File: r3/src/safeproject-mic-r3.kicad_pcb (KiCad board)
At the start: 2 copper layers, 30.5 x 22 mm, 23 parts, among them J101 2842142-4, U101 PCMD3180

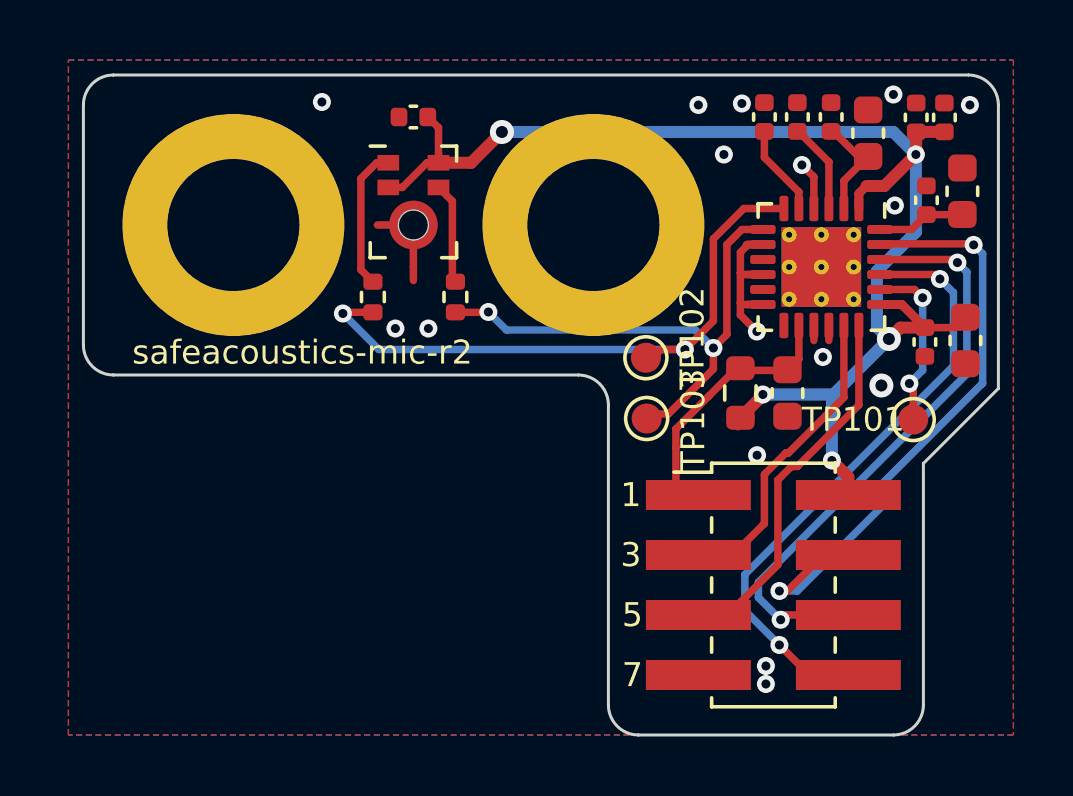
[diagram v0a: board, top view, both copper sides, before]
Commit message: Add fiducials. Change text, move to mask layer.
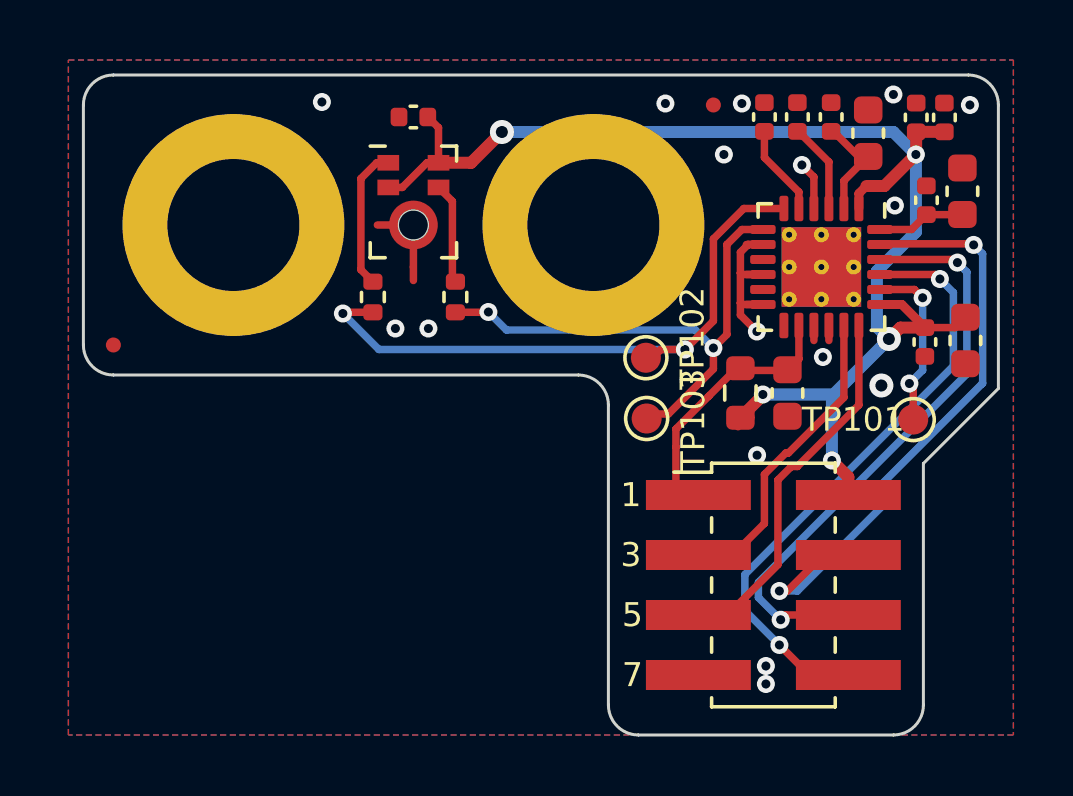
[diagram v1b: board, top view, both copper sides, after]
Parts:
- added FID1: Fiducial, Fiducial:Fiducial_0.5mm_Mask1mm, F.Cu at (10.0, -4.00)
- added FID2: Fiducial, Fiducial:Fiducial_0.5mm_Mask1mm, F.Cu at (-10.0, 4.00)
- C112: value 10uF -> 1uF
- R103: value 10k -> 100k
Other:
- board text added: "bugg-mic-r3"
- board text removed: "safeacoustics-mic-r2"

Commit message: Connect Wurth spacer mounting pads to GND
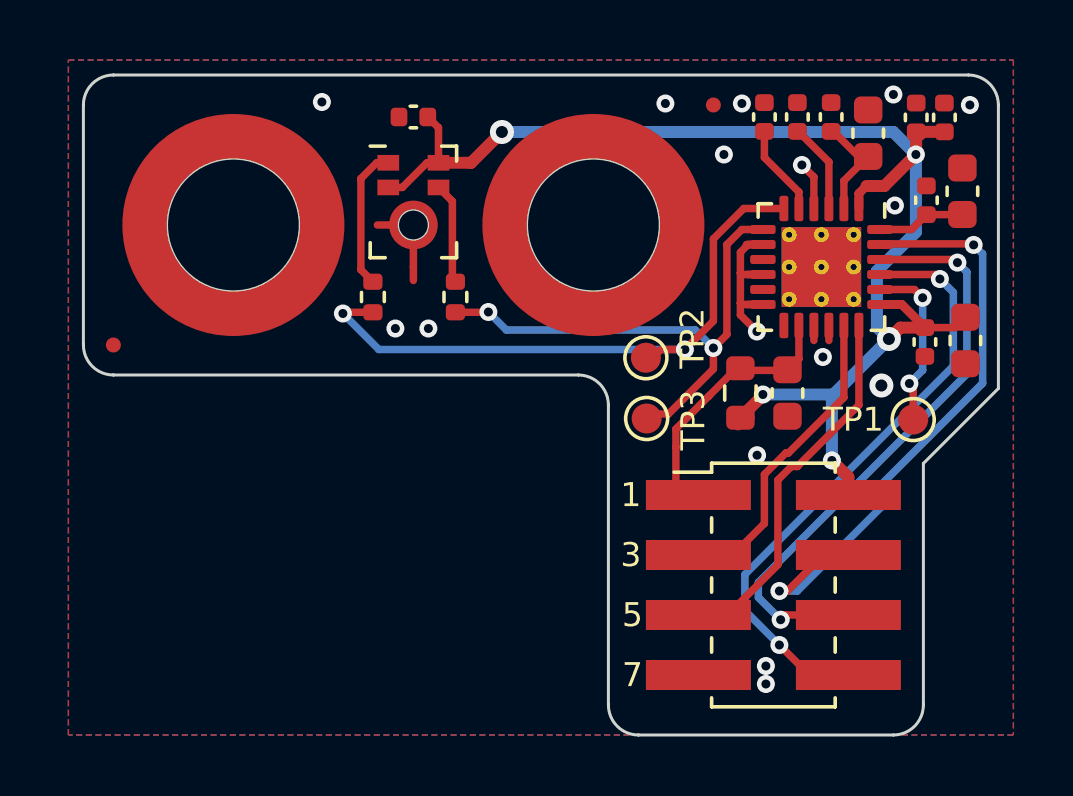
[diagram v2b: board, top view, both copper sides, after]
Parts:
- H101, H102: footprint jeffmakes-footprints:wurth-spacer-WA-SMSI-9774070360R -> Mounting_Wuerth:Mounting_Wuerth_WA-SMSI-M3_H7mm_9774070360
- renumbered TP101 to TP1, TP102 to TP2, TP103 to TP3

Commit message: Shorten test point names
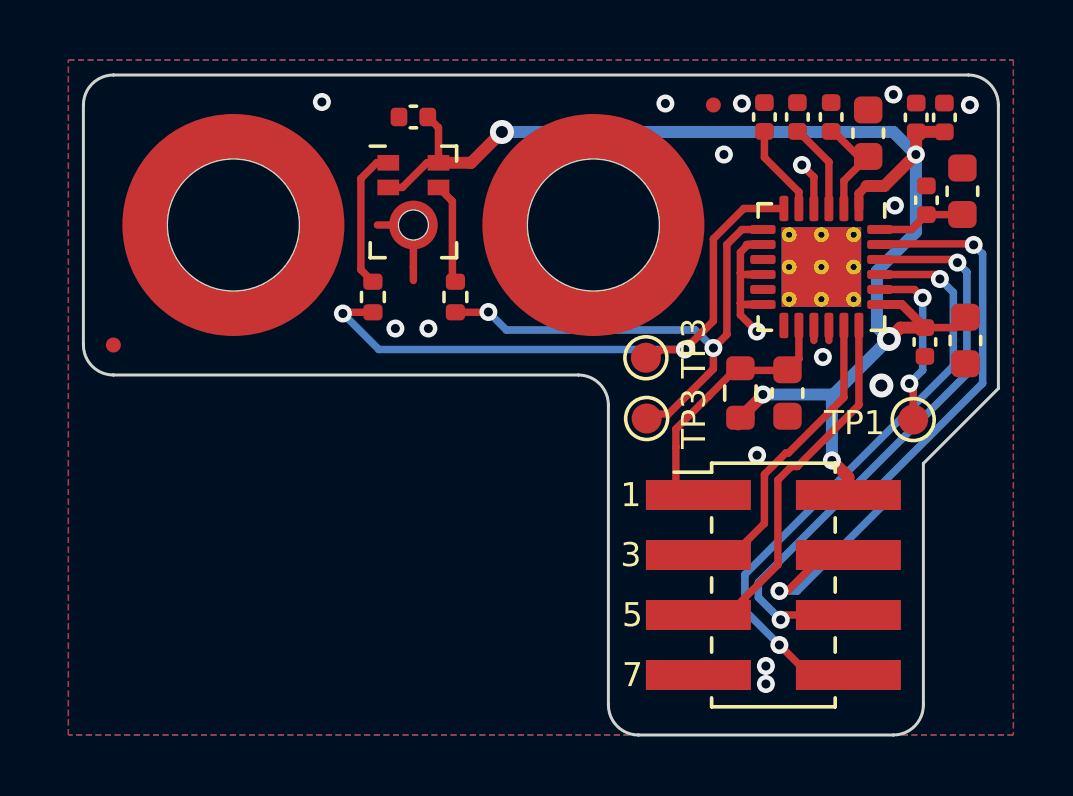
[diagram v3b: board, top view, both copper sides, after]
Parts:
- renumbered TP1 to TP101, TP2 to TP102, TP3 to TP103
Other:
- board text added: "TP1"
- board text added: "TP3"
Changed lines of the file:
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@@
   (net 18 "unconnected-(U101-Pad11)")
   (net 19 "unconnected-(U101-Pad13)")
-  (net 20 "Net-(TP1-Pad1)")
+  (net 20 "Net-(TP101-Pad1)")
   (footprint "Capacitor_SMD:C_0402_1005Metric" (layer "F.Cu")
     (at 12.8 -3.6 -90)
@@
     (property "Sheetname" "")
     (attr exclude_from_pos_files)
-    (fp_text reference "TP1" (at -2 0) (layer "F.SilkS")
+    (fp_text reference "TP101" (at -2 0) (layer "F.SilkS") hide
       (effects (font (size 0.8 0.8) (thickness 0.15)))
     )
@@
     (fp_circle (center 0 0) (end 1 0) (layer "F.CrtYd") (width 0.05) (fill none))
     (pad "1" smd circle locked (at 0 0) (size 1 1) (layers "F.Cu" "F.Mask")
-      (net 20 "Net-(TP1-Pad1)") (pinfunction "1") (pintype "passive"))
+      (net 20 "Net-(TP101-Pad1)") (pinfunction "1") (pintype "passive"))
   )
   (footprint "Capacitor_SMD:C_0603_1608Metric" (layer "F.Cu")
@@
     (property "Sheetname" "")
     (attr exclude_from_pos_files)
-    (fp_text reference "TP3" (at 1.55 0.05 90) (layer "F.SilkS")
+    (fp_text reference "TP103" (at 1.55 0.05 90) (layer "F.SilkS") hide
       (effects (font (size 0.8 0.8) (thickness 0.15)))
     )
@@
       (net 3 "+3V3") (pinfunction "IOVDD") (pintype "power_in"))
     (pad "20" smd roundrect locked (at 0.75 -1.95 270) (size 0.3 0.85) (layers "F.Cu" "F.Paste" "F.Mask") (roundrect_rratio 0.25)
-      (net 20 "Net-(TP1-Pad1)") (pinfunction "GPIO1") (pintype "bidirectional"))
+      (net 20 "Net-(TP101-Pad1)") (pinfunction "GPIO1") (pintype "bidirectional"))
     (pad "21" smd roundrect locked (at 0.25 -1.95 270) (size 0.3 0.85) (layers "F.Cu" "F.Paste" "F.Mask") (roundrect_rratio 0.25)
       (net 7 "/SDOUT") (pinfunction "SDOUT") (pintype "output"))
@@
     (property "Sheetname" "")
     (attr exclude_from_pos_files)
-    (fp_text reference "TP2" (at 1.55 -0.65 90) (layer "F.SilkS")
+    (fp_text reference "TP102" (at 1.55 -0.65 90) (layer "F.SilkS") hide
       (effects (font (size 0.8 0.8) (thickness 0.15)))
     )
@@
   (gr_line (start -11 4) (end -11 -4) (layer "Edge.Cuts") (width 0.1))
   (gr_circle (center 0 0) (end 3 0) (layer "User.1") (width 0.15) (fill none))
+  (gr_text "TP3\n" (at 9.35 4.1 90) (layer "F.SilkS")
+    (effects (font (size 0.8 0.8) (thickness 0.15)))
+  )
   (gr_text "5" (at 7.3 13) (layer "F.SilkS")
     (effects (font (size 0.8 0.8) (thickness 0.15)))
@@
     (effects (font (size 0.8 0.8) (thickness 0.15)))
   )
+  (gr_text "TP3\n" (at 9.35 6.45 90) (layer "F.SilkS")
+    (effects (font (size 0.8 0.8) (thickness 0.15)))
+  )
   (gr_text "3" (at 7.25 11) (layer "F.SilkS")
     (effects (font (size 0.8 0.8) (thickness 0.15)))
   )
+  (gr_text "TP1" (at 14.7 6.6) (layer "F.SilkS")
+    (effects (font (size 0.8 0.8) (thickness 0.15)))
+  )

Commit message: Move fiducial and GND via out of the way of the mousebite area
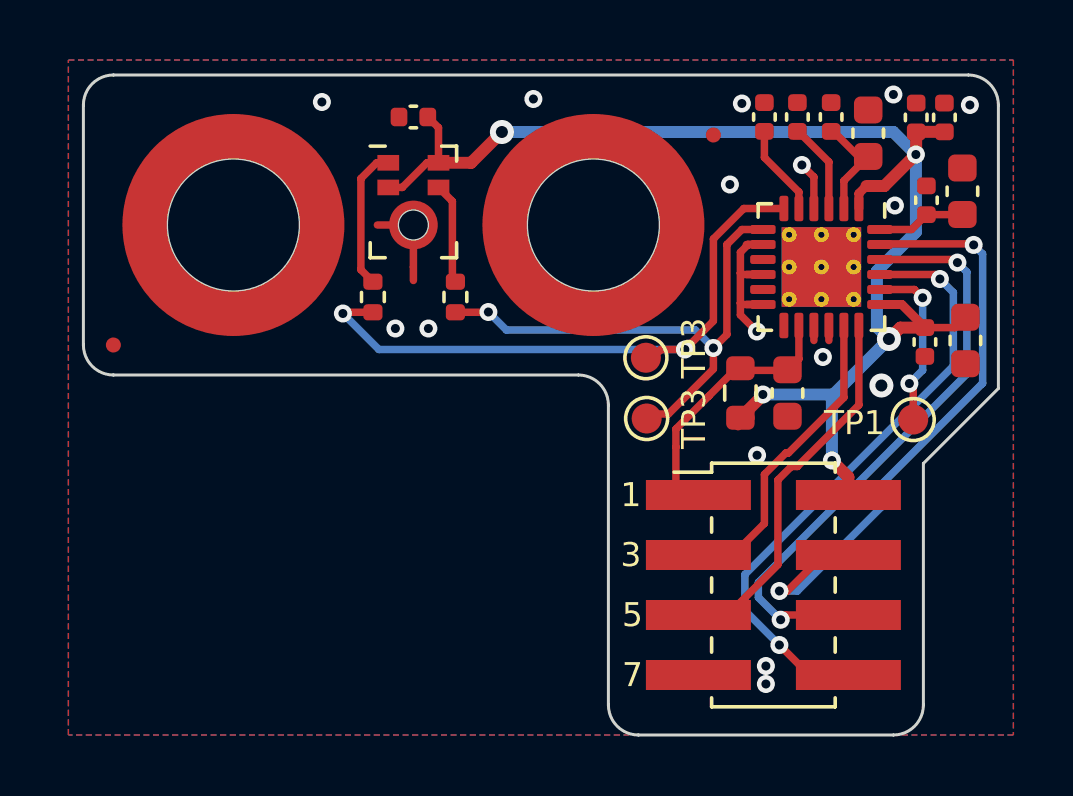
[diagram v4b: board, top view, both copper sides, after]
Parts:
- moved FID1 1.00 mm to (10.0, -3.00)
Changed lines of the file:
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@@
   )
   (footprint "Fiducial:Fiducial_0.5mm_Mask1mm" (layer "F.Cu")
-    (at 10 -4)
+    (at 10 -3)
     (descr "Circular Fiducial, 0.5mm bare copper, 1mm soldermask opening (Level C)")
     (tags "fiducial")
@@
   (via (at 11.75 15.3) (size 0.6) (drill 0.3) (layers "F.Cu" "B.Cu") (net 1))
   (via (at 16 -4.35) (size 0.6) (drill 0.3) (layers "F.Cu" "B.Cu") (net 1))
-  (via (at 10.35 -2.35) (size 0.6) (drill 0.3) (layers "F.Cu" "B.Cu") (net 1))
+  (via (at 10.55 -1.35) (size 0.6) (drill 0.3) (layers "F.Cu" "B.Cu") (net 1))
   (via (at -3.05 -4.1) (size 0.6) (drill 0.3) (layers "F.Cu" "B.Cu") (net 1))
   (via (at 16.04999 -0.65) (size 0.6) (drill 0.3) (layers "F.Cu" "B.Cu") (net 1))
   (via (at 18.55 -4) (size 0.6) (drill 0.3) (layers "F.Cu" "B.Cu") (net 1))
   (via (at 11.455944 7.673746) (size 0.6) (drill 0.3) (layers "F.Cu" "B.Cu") (net 1))
-  (via (at 8.4 -4.05) (size 0.6) (drill 0.3) (layers "F.Cu" "B.Cu") (net 1))
+  (via (at 4 -4.2) (size 0.6) (drill 0.3) (layers "F.Cu" "B.Cu") (net 1))
   (via (at 11.45 3.55) (size 0.6) (drill 0.3) (layers "F.Cu" "B.Cu") (net 1))
   (via (at 10.95 -4.05) (size 0.6) (drill 0.3) (layers "F.Cu" "B.Cu") (net 1))
